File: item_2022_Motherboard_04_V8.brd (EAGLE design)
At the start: 160 x 100 mm, 126 parts, among them IC1 MCP602SN, IC2 LD117AS33TR, IC3 MCP1525TO, IC4 MCP6S28DIL, IC5 MCP6004SO, IC6 MCP6004SO, IC7 MCP3204SL, IC8 LM336LP, IC9 MCP6004SO, U1 ESP32-DEVKITC-32D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

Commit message: FrontEnd con PE
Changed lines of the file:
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@@
 <attribute name="MF" value="" x="39.37" y="10.16" size="1.778" layer="27" rot="R180" display="off"/>
 <attribute name="MPN" value="" x="39.37" y="10.16" size="1.778" layer="27" rot="R180" display="off"/>
-<attribute name="NAME" x="48.2854" y="-5.08" size="1.778" layer="25" ratio="10" rot="R180"/>
+<attribute name="NAME" x="18.7579" y="10.795" size="1.778" layer="25" ratio="10" rot="R180"/>
 <attribute name="OC_FARNELL" value="unknown" x="39.37" y="10.16" size="1.778" layer="27" rot="R180" display="off"/>
 <attribute name="OC_NEWARK" value="unknown" x="39.37" y="10.16" size="1.778" layer="27" rot="R180" display="off"/>

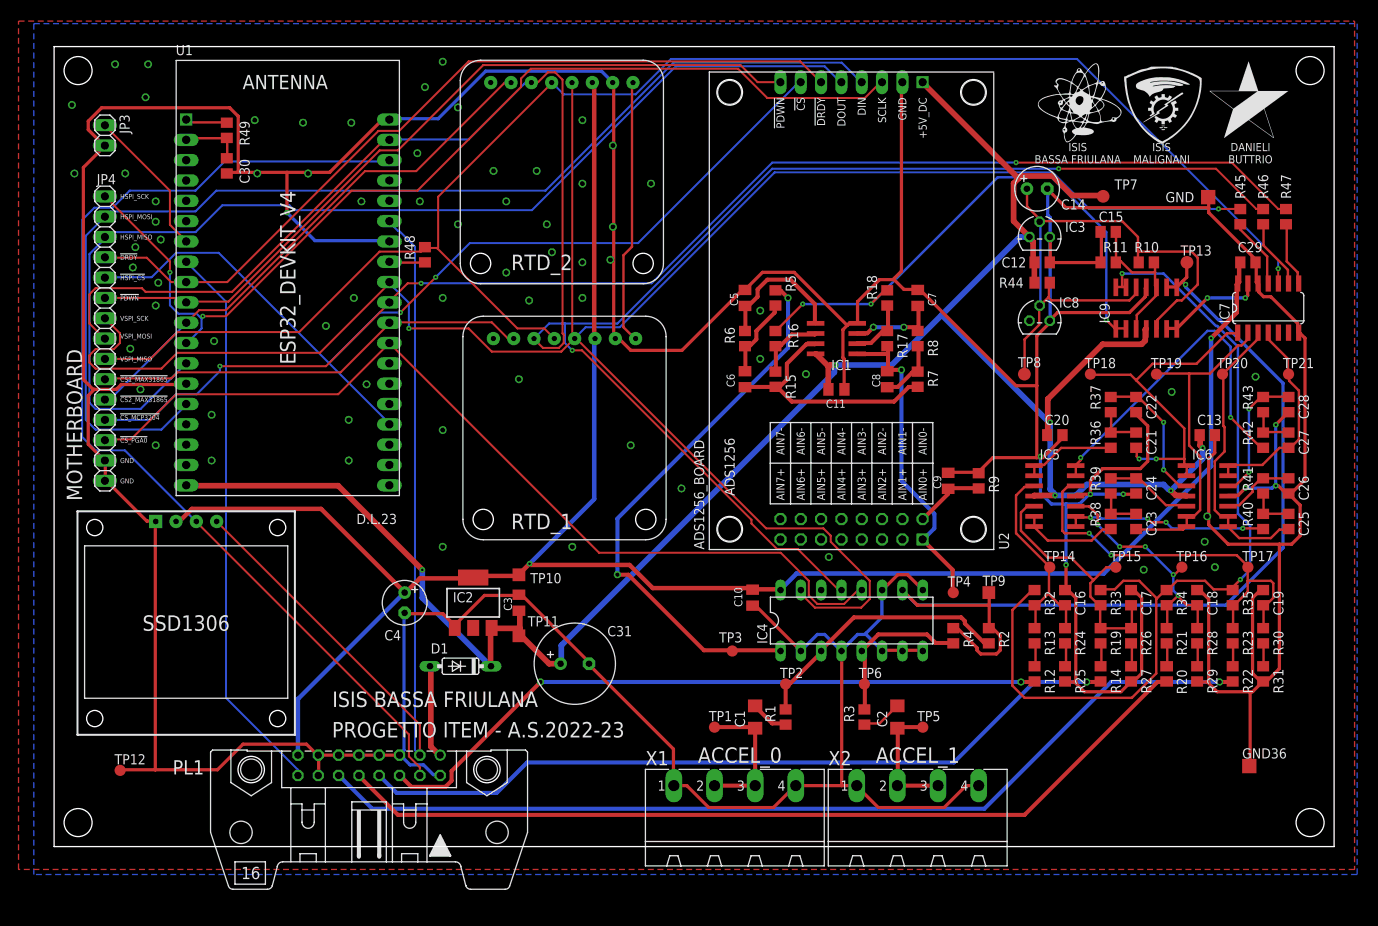
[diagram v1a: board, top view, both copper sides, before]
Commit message: corretto diametro SSD1306 e RTD
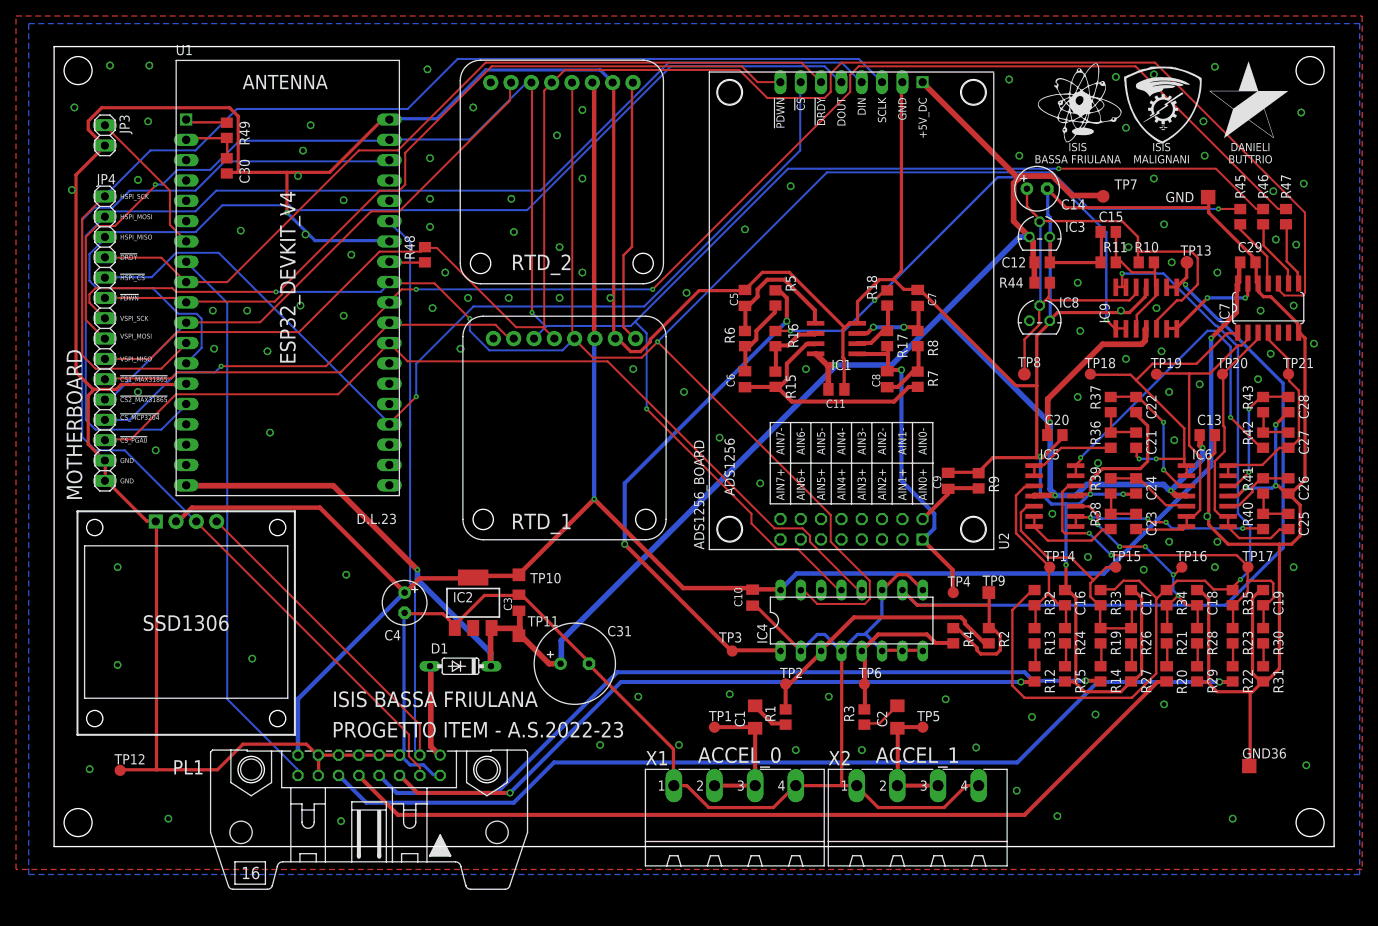
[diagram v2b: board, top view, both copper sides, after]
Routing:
- net VSPI_MISO: track 200.0 -> 219.6 mm, vias 1 -> 0
- net VSPI_SCK: track 269.3 -> 251.3 mm, vias 2 -> 4
- net HSPI_SCK: track 126.6 -> 141.6 mm, vias 2 -> 0
- net !CS_MCP3204!: track 163.8 -> 174.7 mm
- net VSPI_MOSI: track 267.4 -> 256.8 mm, vias 2 -> 4
- net HSPI_MISO: track 138.6 -> 130.9 mm
- net +3V3: track 260.4 -> 255.8 mm
- net N$5: track 69.8 -> 66.0 mm
- net !HSPI_CS!: track 119.3 -> 122.3 mm, vias 2 -> 1
- net !PDWN!: track 97.9 -> 100.5 mm
- net !CS_PGA0!: track 115.0 -> 112.9 mm
- net !CS2_MAX31865!: track 67.2 -> 68.4 mm
- net GND: track 885.4 -> 886.4 mm, vias 76 -> 121
- net TORQUE2+: track 96.9 -> 97.8 mm
- net ADC_HALF_VREF_B: track 68.9 -> 68.2 mm
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
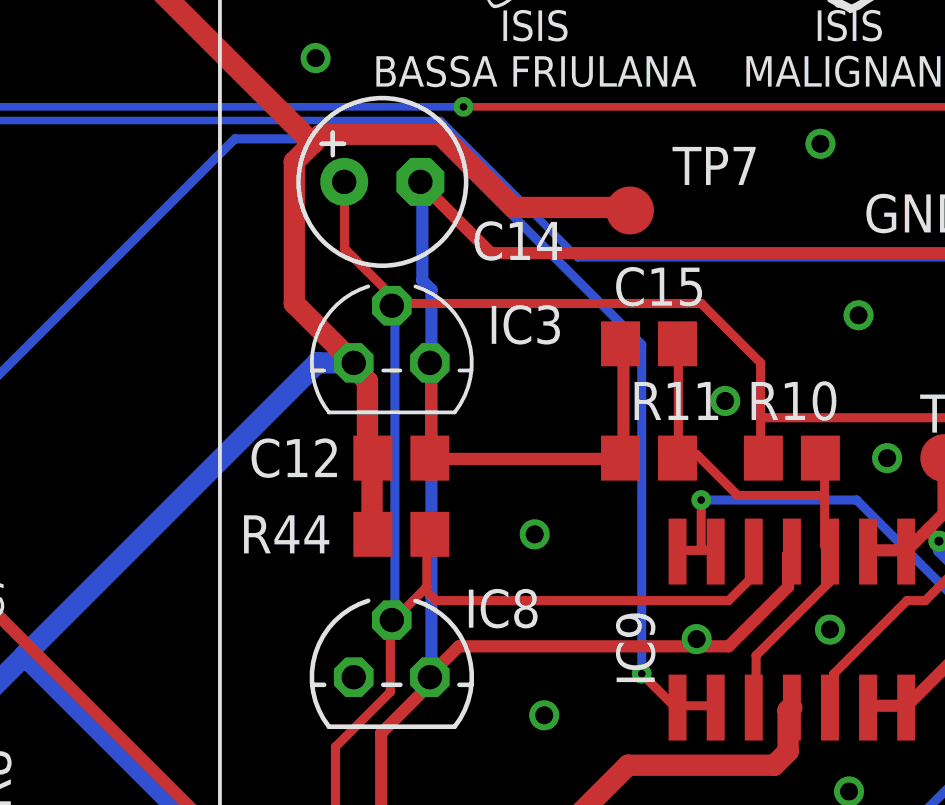
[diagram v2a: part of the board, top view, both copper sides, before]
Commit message: Corretto pinout MCP1525
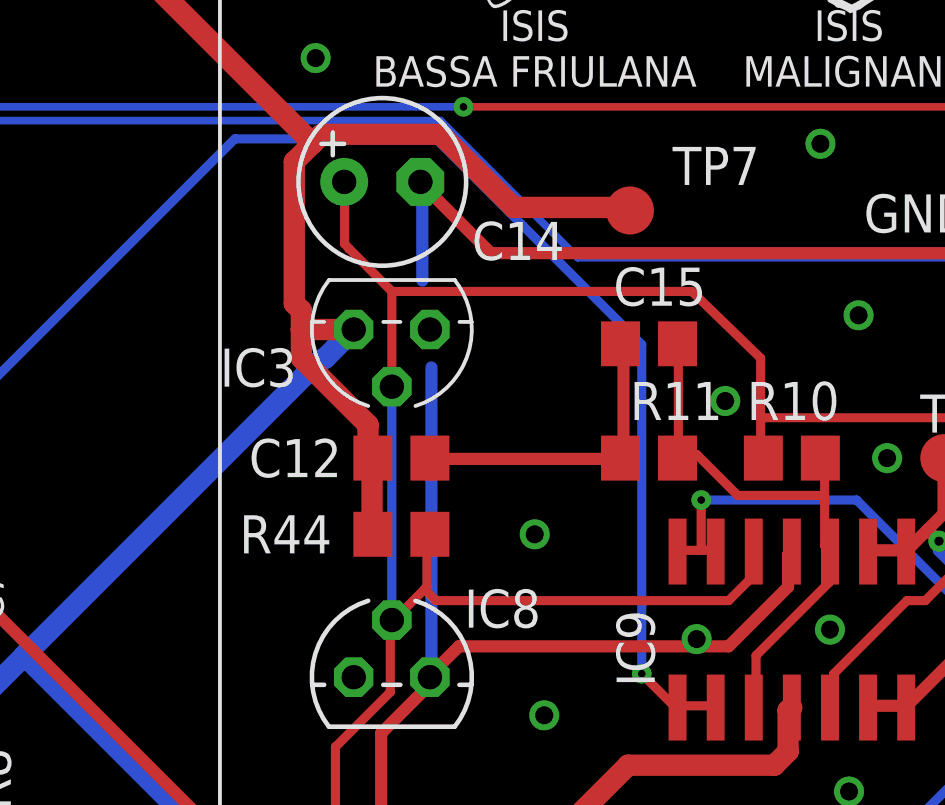
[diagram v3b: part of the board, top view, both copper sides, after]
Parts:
- moved IC3 1.11 mm to (123.2, 77.3), turned to 180 degrees
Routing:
- net GND: track 886.4 -> 880.3 mm
- net +5V: track 278.1 -> 280.6 mm
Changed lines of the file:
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@@
 <param name="RoutingGrid" value="50mil"/>
 <param name="AutoGrid" value="1"/>
-<param name="Efforts" value="2"/>
+<param name="Efforts" value="1"/>
 <param name="TopRouterVariant" value="1"/>
 <param name="tpViaShape" value="round"/>
@@
 <attribute name="VALUE" x="48.2854" y="-2.54" size="1.778" layer="27" ratio="10" rot="R180"/>
 </element>
-<element name="IC3" library="MCP1525_MCP1541" package="TO92" value="MCP1525TO" x="123.19" y="76.2" smashed="yes">
-<attribute name="NAME" x="126.365" y="76.835" size="1.27" layer="25" ratio="10"/>
-<attribute name="VALUE" x="126.365" y="74.93" size="1.27" layer="27" ratio="10"/>
+<element name="IC3" library="MCP1525_MCP1541" package="TO92" value="MCP1525TO" x="123.19" y="77.31125" smashed="yes" rot="R180">
+<attribute name="NAME" x="120.015" y="76.67625" size="1.27" layer="25" ratio="10" rot="R180"/>
+<attribute name="VALUE" x="120.015" y="78.58125" size="1.27" layer="27" ratio="10" rot="R180"/>
 </element>
 <element name="C12" library="rcl_LargePads" package="C0805" value="100nF" x="123.5075" y="73.025" smashed="yes">
@@
 <contactref element="PL1" pad="5"/>
 <contactref element="PL1" pad="14"/>
-<contactref element="IC3" pad="1"/>
 <contactref element="C12" pad="2"/>
 <contactref element="C13" pad="2"/>
@@
 <wire x1="130.9116" y1="73.152" x2="130.8125" y2="73.025" width="0.4064" layer="1"/>
 <wire x1="130.9116" y1="76.8096" x2="130.8125" y2="76.835" width="0.4064" layer="1"/>
-<wire x1="124.5108" y1="76.2" x2="124.5108" y2="73.152" width="0.4064" layer="1"/>
 <wire x1="124.5108" y1="73.152" x2="124.4575" y2="73.025" width="0.4064" layer="1"/>
-<wire x1="124.5108" y1="76.2" x2="124.46" y2="76.2" width="0.4064" layer="1"/>
 <wire x1="124.6632" y1="72.9996" x2="130.7592" y2="72.9996" width="0.4064" layer="1"/>
 <wire x1="130.7592" y1="72.9996" x2="130.8125" y2="73.025" width="0.4064" layer="1"/>
 <wire x1="124.6632" y1="72.9996" x2="124.4575" y2="73.025" width="0.4064" layer="1"/>
 <wire x1="124.206" y1="78.9432" x2="124.206" y2="82.1436" width="0.4064" layer="16"/>
-<wire x1="124.5108" y1="78.6384" x2="124.206" y2="78.9432" width="0.4064" layer="16"/>
-<wire x1="124.5108" y1="76.2" x2="124.5108" y2="78.6384" width="0.4064" layer="16"/>
 <wire x1="124.206" y1="82.1436" x2="124.1425" y2="82.2325" width="0.4064" layer="16"/>
-<wire x1="124.5108" y1="76.2" x2="124.46" y2="76.2" width="0.4064" layer="16"/>
 <wire x1="136.398" y1="68.7324" x2="136.398" y2="69.7992" width="0.4064" layer="1"/>
 <wire x1="134.4168" y1="66.7512" x2="136.398" y2="68.7324" width="0.4064" layer="1"/>
@@
 <wire x1="124.5108" y1="65.8368" x2="124.46" y2="65.7225" width="0.4064" layer="1"/>
 <wire x1="124.5108" y1="65.8368" x2="124.5108" y2="76.0476" width="0.4064" layer="16"/>
-<wire x1="124.5108" y1="76.0476" x2="124.46" y2="76.2" width="0.4064" layer="16"/>
 <wire x1="124.5108" y1="65.8368" x2="124.46" y2="65.7225" width="0.4064" layer="16"/>
 <wire x1="122.8344" y1="63.8556" x2="122.8344" y2="57.6072" width="0.4064" layer="1"/>
@@
 <via x="7.9375" y="22.70125" extent="1-16" drill="0.6"/>
 <via x="7.9375" y="34.925" extent="1-16" drill="0.6"/>
+<contactref element="IC3" pad="1"/>
 </signal>
 <signal name="+5V" class="4">
@@
 <contactref element="IC1" pad="8"/>
 <contactref element="C11" pad="1"/>
-<contactref element="IC3" pad="3"/>
 <contactref element="C12" pad="1"/>
 <contactref element="C13" pad="1"/>
@@
 <wire x1="120.5484" y1="83.5152" x2="120.8532" y2="83.82" width="0.7112" layer="1"/>
 <wire x1="119.9388" y1="78.1812" x2="119.9388" y2="82.9056" width="0.7112" layer="1"/>
-<wire x1="121.92" y1="76.2" x2="119.9388" y2="78.1812" width="0.7112" layer="1"/>
 <wire x1="131.064" y1="81.3816" x2="131.1275" y2="81.28" width="0.7112" layer="1"/>
-<wire x1="122.3772" y1="75.5904" x2="122.3772" y2="73.3044" width="0.7112" layer="1"/>
-<wire x1="122.0724" y1="75.8952" x2="122.3772" y2="75.5904" width="0.7112" layer="1"/>
 <wire x1="122.3772" y1="73.3044" x2="122.5575" y2="73.025" width="0.7112" layer="1"/>
-<wire x1="122.0724" y1="75.8952" x2="121.92" y2="76.2" width="0.7112" layer="1"/>
 <wire x1="120.5484" y1="83.5152" x2="108.6612" y2="95.4024" width="0.7112" layer="1"/>
 <wire x1="108.6612" y1="95.4024" x2="108.57" y2="95.55" width="0.7112" layer="1"/>
@@
 <wire x1="120.7008" y1="76.2" x2="110.9472" y2="66.4464" width="0.7112" layer="16"/>
 <wire x1="110.9472" y1="66.4464" x2="104.6988" y2="60.198" width="0.7112" layer="16"/>
-<wire x1="121.92" y1="76.2" x2="120.7008" y2="76.2" width="0.7112" layer="16"/>
 <wire x1="97.0788" y1="60.198" x2="96.774" y2="60.0456" width="0.7112" layer="1"/>
 <wire x1="110.9472" y1="66.4464" x2="124.206" y2="53.1876" width="0.7112" layer="16"/>
@@
 <via x="124.5108" y="53.0352" extent="1-16" drill="0.3048"/>
 <via x="97.6884" y="60.198" extent="1-16" drill="0.3048"/>
+<contactref element="IC3" pad="3"/>
+<wire x1="120.9675" y1="76.35875" x2="121.92" y2="77.31125" width="0.7112" layer="16"/>
+<wire x1="120.9675" y1="76.35875" x2="120.7008" y2="76.2" width="0.7112" layer="16"/>
+<wire x1="122.39625" y1="74.13625" x2="122.39625" y2="73.66" width="0.7112" layer="1"/>
+<wire x1="120.17375" y1="76.35875" x2="122.39625" y2="74.13625" width="0.7112" layer="1"/>
+<wire x1="120.17375" y1="77.94625" x2="120.17375" y2="77.31125" width="0.7112" layer="1"/>
+<wire x1="120.17375" y1="77.31125" x2="120.17375" y2="76.35875" width="0.7112" layer="1"/>
+<wire x1="122.39625" y1="73.66" x2="122.5575" y2="73.025" width="0.7112" layer="1"/>
+<wire x1="120.17375" y1="77.94625" x2="119.9388" y2="78.1812" width="0.7112" layer="1"/>
+<wire x1="120.17375" y1="77.31125" x2="121.92" y2="77.31125" width="0.7112" layer="1"/>
 </signal>
 <signal name="HSPI_SCK" class="2">
@@
 <contactref element="IC8" pad="2"/>
 <contactref element="R44" pad="1"/>
-<contactref element="IC3" pad="2"/>
 <contactref element="R10" pad="2"/>
 <contactref element="IC9" pad="5"/>
@@
 <wire x1="124.2822" y1="68.6562" x2="124.6632" y2="68.2752" width="0.3048" layer="1"/>
 <wire x1="135.1788" y1="69.7992" x2="135.255" y2="69.91" width="0.3048" layer="1"/>
-<wire x1="135.4836" y1="76.2" x2="135.4836" y2="74.3712" width="0.3048" layer="1"/>
+<wire x1="135.4836" y1="76.35875" x2="135.4836" y2="74.3712" width="0.3048" layer="1"/>
 <wire x1="135.4836" y1="74.3712" x2="135.4836" y2="73.152" width="0.3048" layer="1"/>
-<wire x1="133.5024" y1="78.1812" x2="135.4836" y2="76.2" width="0.3048" layer="1"/>
-<wire x1="123.2916" y1="78.1812" x2="133.5024" y2="78.1812" width="0.3048" layer="1"/>
 <wire x1="135.4836" y1="73.152" x2="135.575" y2="73.025" width="0.3048" layer="1"/>
-<wire x1="123.2916" y1="78.1812" x2="123.19" y2="78.105" width="0.3048" layer="1"/>
 <wire x1="137.922" y1="65.8368" x2="137.922" y2="64.77" width="0.3048" layer="1"/>
 <wire x1="140.3604" y1="68.2752" x2="137.922" y2="65.8368" width="0.3048" layer="1"/>
@@
 <wire x1="135.4836" y1="74.3712" x2="142.1892" y2="74.3712" width="0.3048" layer="1"/>
 <wire x1="137.922" y1="64.77" x2="137.795" y2="64.71" width="0.3048" layer="1"/>
-<wire x1="121.6152" y1="80.01" x2="121.6152" y2="82.1436" width="0.3048" layer="1"/>
-<wire x1="123.2916" y1="78.3336" x2="121.6152" y2="80.01" width="0.3048" layer="1"/>
+<wire x1="121.6152" y1="80.16875" x2="121.6152" y2="82.1436" width="0.3048" layer="1"/>
 <wire x1="121.6152" y1="82.1436" x2="121.6025" y2="82.2325" width="0.3048" layer="1"/>
-<wire x1="123.2916" y1="78.3336" x2="123.19" y2="78.105" width="0.3048" layer="1"/>
-<wire x1="123.2916" y1="78.0288" x2="123.2916" y2="67.6656" width="0.3048" layer="16"/>
 <wire x1="123.2916" y1="67.6656" x2="123.19" y2="67.6275" width="0.3048" layer="16"/>
-<wire x1="123.2916" y1="78.0288" x2="123.19" y2="78.105" width="0.3048" layer="16"/>
+<contactref element="IC3" pad="2"/>
+<wire x1="123.19" y1="78.58125" x2="123.19" y2="75.40625" width="0.3048" layer="1"/>
+<wire x1="121.76125" y1="80.01" x2="123.19" y2="78.58125" width="0.3048" layer="1"/>
+<wire x1="121.76125" y1="80.01" x2="121.6152" y2="80.16875" width="0.3048" layer="1"/>
+<wire x1="123.19" y1="67.6275" x2="123.19" y2="75.40625" width="0.3048" layer="16"/>
+<wire x1="133.19125" y1="78.58125" x2="123.19" y2="78.58125" width="0.3048" layer="1"/>
+<wire x1="133.19125" y1="78.58125" x2="135.4836" y2="76.35875" width="0.3048" layer="1"/>
 </signal>
 <signal name="+2.5V">
